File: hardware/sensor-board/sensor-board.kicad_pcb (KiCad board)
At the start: 4 copper layers, 59.2 x 26.5 mm, 44 parts, among them J1 QWIIC Connector, J2 QWIIC Connector, J3 3-pole terminal, J4 2-pole terminal, Q1 BSS84, SW1 SW_DIP_x03, U2 DS2482S-100+, U3 PCA9501PW_118, U4 LMV601, U5 MCP96L01T-E/MX, U6 ADS7823EB/250

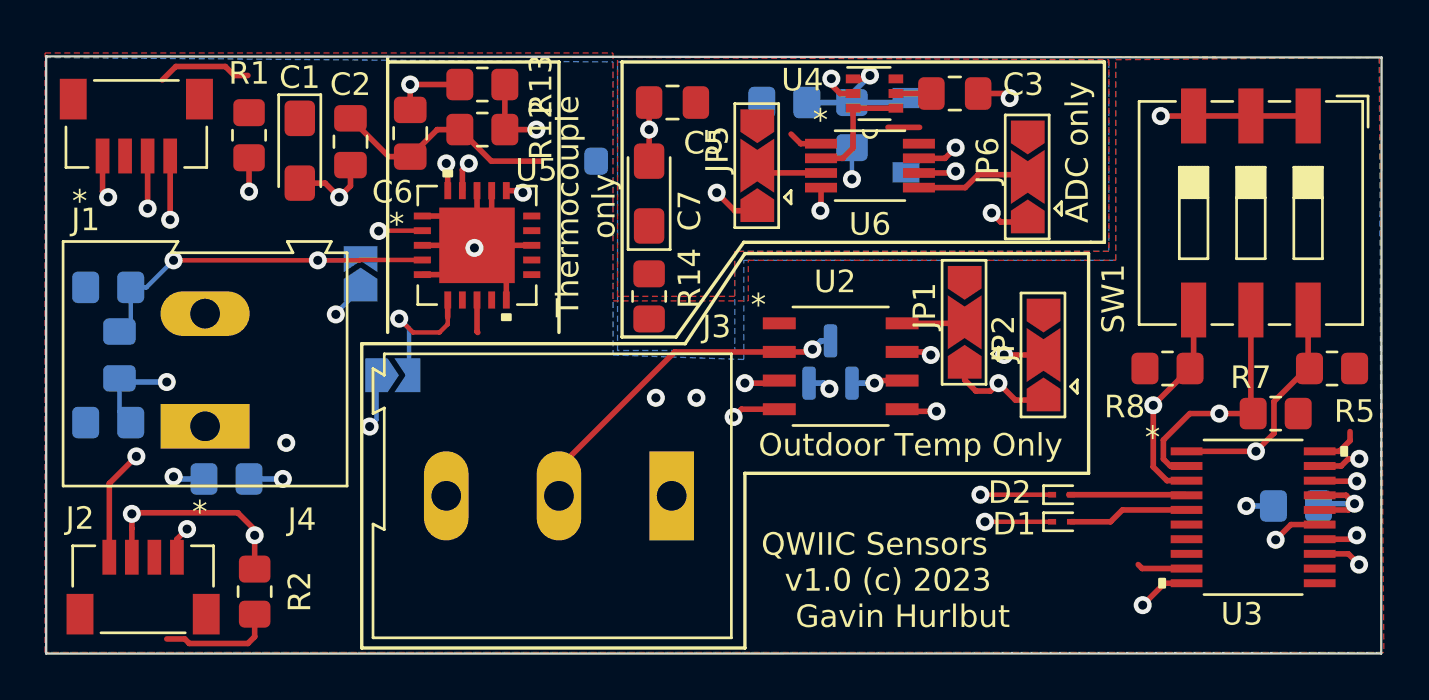
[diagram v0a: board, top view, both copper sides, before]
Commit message: Change coolant sensor to a 10k NTC thermistor
- this requires one more "TBD" resistor to be added to the board.
- regenerated gerbers
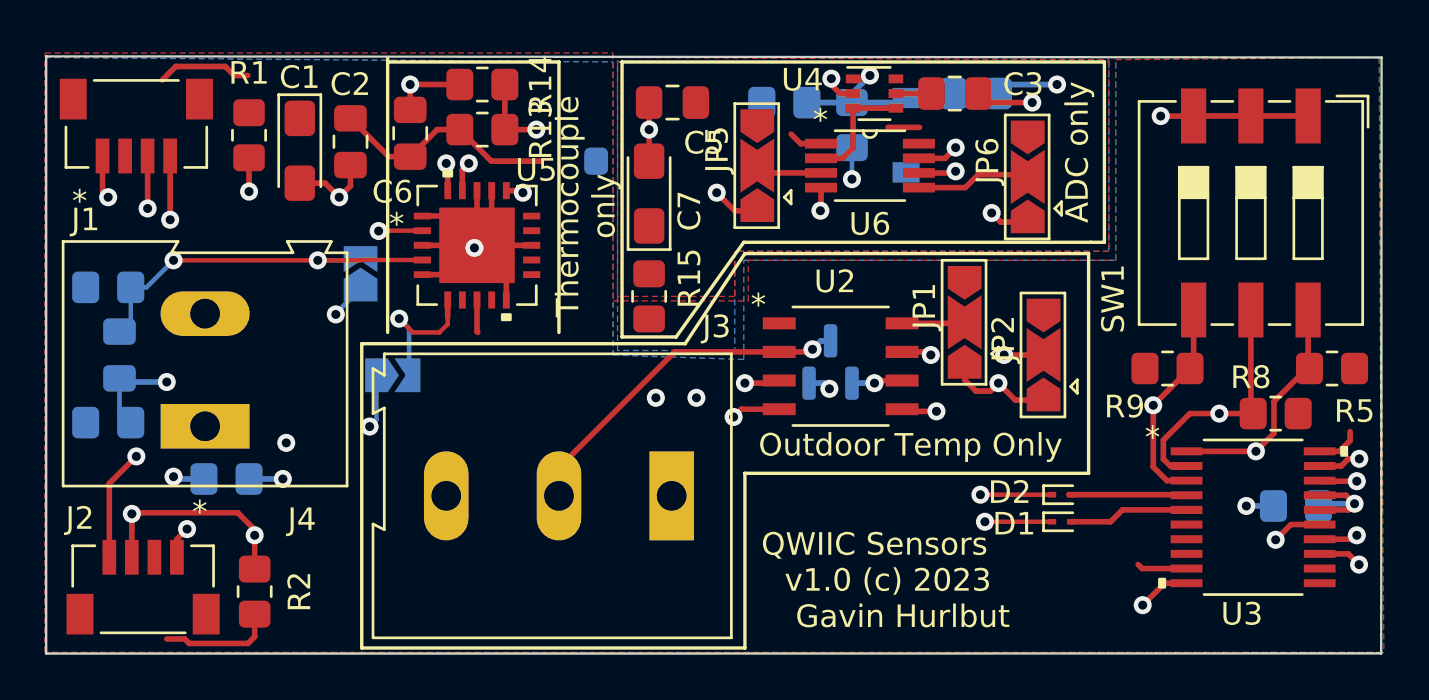
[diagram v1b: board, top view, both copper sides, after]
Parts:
- added R6: TBD, Resistor_SMD:R_0805_2012Metric_Pad1.20x1.40mm_HandSolder, B.Cu at (116.5, 126.4)
- renumbered R9 to R10, R10 to R11, R11 to R12, R12 to R13, R13 to R14, R14 to R15, R6 to R7, R7 to R8, R8 to R9
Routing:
- net +3V3A: track 4.48 -> 7.25 mm, vias 0 -> 1
- net Net-(D3-Pad1): track 6.83 -> 9.01 mm
- net GNDA: track 10.8 -> 11.8 mm
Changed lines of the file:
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@@
   (net 21 "A1")
   (net 22 "A2")
-  (net 23 "Net-(R12-Pad2)")
+  (net 23 "Net-(R13-Pad2)")
   (net 24 "unconnected-(U3-Pad6)")
   (net 25 "unconnected-(U3-Pad7)")
@@
     (property "Sheetname" "")
     (attr smd)
-    (fp_text reference "R7" (at 1.1 1.6) (layer "F.SilkS")
+    (fp_text reference "R8" (at 1.1 1.6) (layer "F.SilkS")
       (effects (font (size 1 1) (thickness 0.15)))
     )
@@
       (net 33 "unconnected-(U5-Pad15)") (pinfunction "ALERT4") (pintype "output+no_connect"))
     (pad "16" smd rect locked (at 1.3 -2.4257) (size 0.3048 0.762) (layers "F.Cu" "F.Paste" "F.Mask")
-      (net 23 "Net-(R12-Pad2)") (pinfunction "ADDR") (pintype "input"))
+      (net 23 "Net-(R13-Pad2)") (pinfunction "ADDR") (pintype "input"))
     (pad "17" smd rect locked (at 0.649999 -2.4257) (size 0.3048 0.762) (layers "F.Cu" "F.Paste" "F.Mask")
       (net 2 "GND") (pinfunction "GND") (pintype "power_in"))
@@
     (property "Sheetname" "")
     (attr smd)
-    (fp_text reference "R12" (at 2.6 0 90) (layer "F.SilkS")
+    (fp_text reference "R13" (at 2.6 0 90) (layer "F.SilkS")
       (effects (font (size 1 1) (thickness 0.15)))
     )
@@
       (net 1 "+3V3") (pintype "passive"))
     (pad "2" smd roundrect (at 1 0) (size 1.2 1.4) (layers "F.Cu" "F.Paste" "F.Mask") (roundrect_rratio 0.2083333333)
-      (net 23 "Net-(R12-Pad2)") (pintype "passive"))
+      (net 23 "Net-(R13-Pad2)") (pintype "passive"))
     (model "${KICAD6_3DMODEL_DIR}/Resistor_SMD.3dshapes/R_0805_2012Metric.wrl"
       (offset (xyz 0 0 0))
@@
     (property "Sheetname" "")
     (attr smd)
-    (fp_text reference "R14" (at 0.8 1.8 90) (layer "F.SilkS")
+    (fp_text reference "R15" (at 0.8 1.8 90) (layer "F.SilkS")
       (effects (font (size 1 1) (thickness 0.15)))
     )
@@
     (property "Sheetname" "")
     (attr smd)
-    (fp_text reference "R8" (at -1.9 1.7) (layer "F.SilkS")
+    (fp_text reference "R9" (at -1.9 1.7) (layer "F.SilkS")
       (effects (font (size 1 1) (thickness 0.15)))
     )
@@
     (property "Sheetname" "")
     (attr smd)
-    (fp_text reference "R13" (at -2.6 0 90) (layer "F.SilkS")
+    (fp_text reference "R14" (at -2.6 0 90) (layer "F.SilkS")
       (effects (font (size 1 1) (thickness 0.15)))
     )
@@
     (fp_line (start -1 0.625) (end -1 -0.625) (layer "F.Fab") (width 0.1))
     (pad "1" smd roundrect (at -1 0 180) (size 1.2 1.4) (layers "F.Cu" "F.Paste" "F.Mask") (roundrect_rratio 0.2083333333)
-      (net 23 "Net-(R12-Pad2)") (pintype "passive"))
+      (net 23 "Net-(R13-Pad2)") (pintype "passive"))
     (pad "2" smd roundrect (at 1 0 180) (size 1.2 1.4) (layers "F.Cu" "F.Paste" "F.Mask") (roundrect_rratio 0.2083333333)
       (net 2 "GND") (pintype "passive"))
@@
     )
   )
+  (footprint "Resistor_SMD:R_0805_2012Metric_Pad1.20x1.40mm_HandSolder" (layer "B.Cu")
+    (at 116.5 126.4 180)
+    (descr "Resistor SMD 0805 (2012 Metric), square (rectangular) end terminal, IPC_7351 nominal with elongated pad for handsoldering. (Body size source: IPC-SM-782 page 72, https://www.pcb-3d.com/wordpress/wp-content/uploads/ipc-sm-782a_amendment_1_and_2.pdf), generated with kicad-footprint-generator")
+    (tags "resistor handsolder")
+    (property "Sheetfile" "sensor-board.kicad_sch")
+    (property "Sheetname" "")
+    (attr smd)
+    (fp_text reference "R6" (at -0.4 -1.8) (layer "B.SilkS")
+      (effects (font (size 1 1) (thickness 0.15)) (justify mirror))
+    )
+    (fp_text value "TBD" (at 0 -1.65) (layer "B.Fab")
+      (effects (font (size 1 1) (thickness 0.15)) (justify mirror))
+    )
+    (fp_text user "${REFERENCE}" (at 0 0) (layer "B.Fab")
+      (effects (font (size 0.5 0.5) (thickness 0.08)) (justify mirror))
+    )
+    (fp_line (start -0.227064 0.735) (end 0.227064 0.735) (layer "B.SilkS") (width 0.12))
+    (fp_line (start -0.227064 -0.735) (end 0.227064 -0.735) (layer "B.SilkS") (width 0.12))
+    (fp_line (start 1.85 -0.95) (end -1.85 -0.95) (layer "B.CrtYd") (width 0.05))
+    (fp_line (start -1.85 0.95) (end 1.85 0.95) (layer "B.CrtYd") (width 0.05))
+    (fp_line (start 1.85 0.95) (end 1.85 -0.95) (layer "B.CrtYd") (width 0.05))
+    (fp_line (start -1.85 -0.95) (end -1.85 0.95) (layer "B.CrtYd") (width 0.05))
+    (fp_line (start 1 0.625) (end 1 -0.625) (layer "B.Fab") (width 0.1))
+    (fp_line (start -1 -0.625) (end -1 0.625) (layer "B.Fab") (width 0.1))
+    (fp_line (start -1 0.625) (end 1 0.625) (layer "B.Fab") (width 0.1))
+    (fp_line (start 1 -0.625) (end -1 -0.625) (layer "B.Fab") (width 0.1))
+    (pad "1" smd roundrect (at -1 0 180) (size 1.2 1.4) (layers "B.Cu" "B.Paste" "B.Mask") (roundrect_rratio 0.208333)
+      (net 6 "+3V3A") (pintype "passive"))
+    (pad "2" smd roundrect (at 1 0 180) (size 1.2 1.4) (layers "B.Cu" "B.Paste" "B.Mask") (roundrect_rratio 0.208333)
+      (net 17 "Net-(D3-Pad1)") (pintype "passive"))
+    (model "${KICAD6_3DMODEL_DIR}/Resistor_SMD.3dshapes/R_0805_2012Metric.wrl"
+      (offset (xyz 0 0 0))
+      (scale (xyz 1 1 1))
+      (rotate (xyz 0 0 0))
+    )
+  )
   (footprint "Jumper:SolderJumper-2_P1.3mm_Open_TrianglePad1.0x1.5mm" (layer "B.Cu")
     (at 89.2 134.4 90)
@@
     (property "Sheetname" "")
     (attr smd)
-    (fp_text reference "R10" (at 0.75 -1.75) (layer "B.SilkS")
+    (fp_text reference "R11" (at 0.75 -1.75) (layer "B.SilkS")
       (effects (font (size 1 1) (thickness 0.15)) (justify mirror))
     )
@@
     (property "Sheetname" "")
     (attr smd)
-    (fp_text reference "R11" (at -3 0.25) (layer "B.SilkS")
+    (fp_text reference "R12" (at -3 0.25) (layer "B.SilkS")
       (effects (font (size 1 1) (thickness 0.15)) (justify mirror))
     )
@@
     (property "Sheetname" "")
     (attr smd)
-    (fp_text reference "R9" (at -0.65 -1.6 180) (layer "B.SilkS")
+    (fp_text reference "R10" (at -0.65 -1.6 180) (layer "B.SilkS")
       (effects (font (size 1 1) (thickness 0.15)) (justify mirror))
     )
@@
     (property "Sheetname" "")
     (attr smd)
-    (fp_text reference "R6" (at 1 -1.8) (layer "B.SilkS")
+    (fp_text reference "R7" (at 1 -1.8) (layer "B.SilkS")
       (effects (font (size 1 1) (thickness 0.15)) (justify mirror))
     )
@@
   (segment (start 102 127.2375) (end 101.7625 127) (width 0.25) (layer "F.Cu") (net 5))
   (segment (start 118.8 132.1) (end 117.6 132.1) (width 0.25) (layer "F.Cu") (net 5))
+  (segment (start 117 126.8) (end 116.6 126.4) (width 0.25) (layer "F.Cu") (net 5))
   (segment (start 109.6283 130.574999) (end 109.6283 131.5717) (width 0.25) (layer "F.Cu") (net 5))
   (segment (start 110.475 126.4) (end 110.085493 126.010493) (width 0.25) (layer "F.Cu") (net 5))
-  (segment (start 116.6 126.4) (end 117.8 126.4) (width 0.25) (layer "F.Cu") (net 5))
   (segment (start 105.8 131.6) (end 105 130.8) (width 0.25) (layer "F.Cu") (net 5))
   (segment (start 117.6 132.1) (end 117.2 131.7) (width 0.25) (layer "F.Cu") (net 5))
@@
   (segment (start 111.05 126.4) (end 110.475 126.4) (width 0.25) (layer "F.Cu") (net 5))
   (segment (start 110.085493 126.010493) (end 110.085493 125.738744) (width 0.25) (layer "F.Cu") (net 5))
-  (segment (start 117.8 126.4) (end 118 126.6) (width 0.25) (layer "F.Cu") (net 5))
+  (segment (start 119 126.8) (end 117 126.8) (width 0.25) (layer "F.Cu") (net 5))
   (via (at 117.2 131.7) (size 0.8) (drill 0.4) (layers "F.Cu" "B.Cu") (net 5))
   (via (at 102 128) (size 0.8) (drill 0.4) (layers "F.Cu" "B.Cu") (net 5))
   (via (at 105 130.8) (size 0.8) (drill 0.4) (layers "F.Cu" "B.Cu") (net 5))
   (via (at 110.085493 125.738744) (size 0.8) (drill 0.4) (layers "F.Cu" "B.Cu") (net 5))
-  (via (at 118 126.6) (size 0.8) (drill 0.4) (layers "F.Cu" "B.Cu") (net 5))
+  (via (at 119 126.8) (size 0.8) (drill 0.4) (layers "F.Cu" "B.Cu") (net 5))
   (via (at 109.6 131.6) (size 0.8) (drill 0.4) (layers "F.Cu" "B.Cu") (net 5))
   (segment locked (start 108.725001 128.625001) (end 108.3 128.2) (width 0.25) (layer "F.Cu") (net 6))
@@
   (segment locked (start 112.6 127.9) (end 114 127.9) (width 0.25) (layer "F.Cu") (net 6))
   (segment locked (start 112.95 126.4) (end 114.525 126.4) (width 0.25) (layer "F.Cu") (net 6))
+  (via (at 120.1 126) (size 0.8) (drill 0.4) (layers "F.Cu" "B.Cu") (net 6))
+  (segment (start 117.5 126.4) (end 117.9 126) (width 0.25) (layer "B.Cu") (net 6))
+  (segment (start 117.9 126) (end 120.1 126) (width 0.25) (layer "B.Cu") (net 6))
   (segment (start 93.065 136.635) (end 93.065 136.335) (width 0.2) (layer "F.Cu") (net 7))
   (segment (start 90.912299 136.387701) (end 91.524598 137) (width 0.2) (layer "F.Cu") (net 7))
@@
   (segment (start 111.65 125.75) (end 111.05 125.75) (width 0.25) (layer "F.Cu") (net 17))
   (via (at 111.8 125.6) (size 0.8) (drill 0.4) (layers "F.Cu" "B.Cu") (net 17))
+  (segment (start 113.4 126.6) (end 115.3 126.6) (width 0.25) (layer "B.Cu") (net 17))
   (segment (start 111 126.4) (end 111.8 125.6) (width 0.25) (layer "B.Cu") (net 17))
+  (segment (start 115.3 126.6) (end 115.5 126.4) (width 0.25) (layer "B.Cu") (net 17))
   (segment (start 111 126.8) (end 111 126.4) (width 0.25) (layer "B.Cu") (net 17))
   (segment (start 113.2 126.8) (end 113.4 126.6) (width 0.25) (layer "B.Cu") (net 17))

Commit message: Changed DIP switch to solder jumper pads, regen gerbers
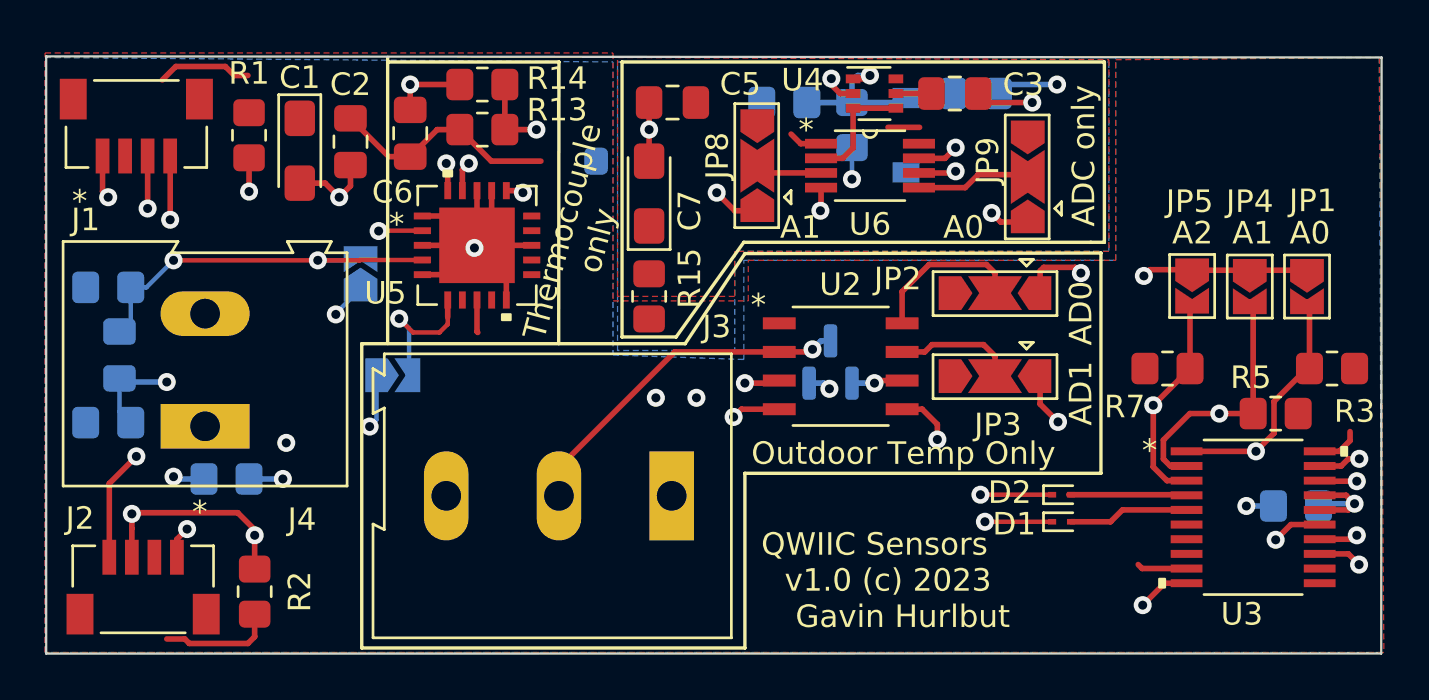
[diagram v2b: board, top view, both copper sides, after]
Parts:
- removed SW1: SW_DIP_x03, Button_Switch_SMD:SW_DIP_SPSTx03_Slide_9.78x9.8mm_W8.61mm_P2.54mm
- added JP1: Solder Jumper, Jumper:SolderJumper-2_P1.3mm_Open_TrianglePad1.0x1.5mm, F.Cu at (131.2, 135.0)
- added JP4: Solder Jumper, Jumper:SolderJumper-2_P1.3mm_Open_TrianglePad1.0x1.5mm, F.Cu at (128.7, 135.0)
- added JP5: Solder Jumper, Jumper:SolderJumper-2_P1.3mm_Open_TrianglePad1.0x1.5mm, F.Cu at (126.1, 134.9)
- moved JP3 2.35 mm to (117.3, 138.9), turned to 180 degrees
- moved JP2 1.87 mm to (117.3, 135.3), turned to 180 degrees
- renumbered JP1 to JP2, JP2 to JP3, JP3 to JP6, JP4 to JP7, JP5 to JP8, JP6 to JP9, R5 to R3, R3 to R4, R8 to R5, R4 to R6, R9 to R7, R6 to R8, R7 to R9
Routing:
- net Net-(JP2-Pad2): track 2.79 -> 7.08 mm
- net GND: track 44.6 -> 45.9 mm, vias 9 -> 10
- net SDA: track 111.7 -> 112.8 mm
- net Net-(JP3-Pad2): track 6.33 -> 5.36 mm, vias 2 -> 0
- net A2: track 20.5 -> 21.0 mm
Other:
- board text added: "A0"
- board text added: "A1"
- board text added: "A2"
- board text added: "AD0"
- board text added: "AD1"
- board text added: "VIN+"
- board text added: "VIN-"

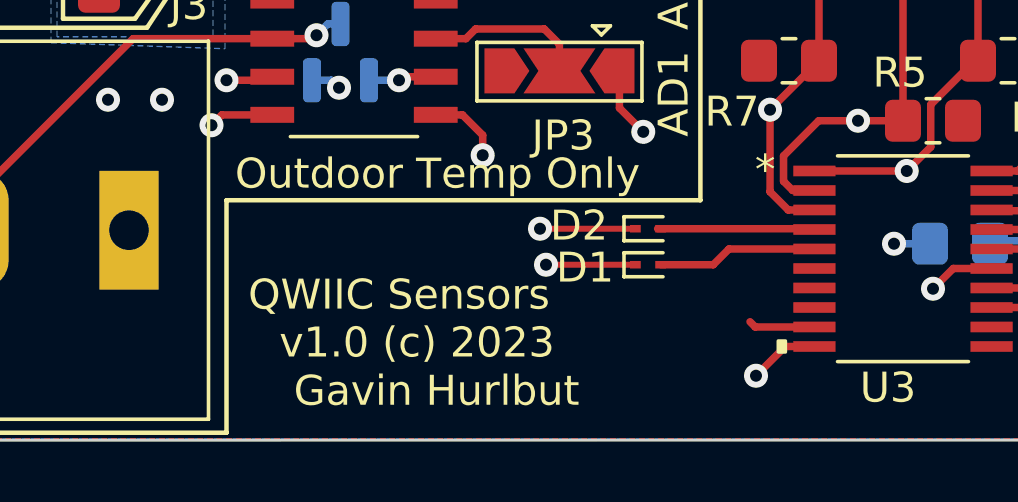
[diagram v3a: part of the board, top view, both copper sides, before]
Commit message: Got rid of TINY diode (0402!?!?), remove USE_USB, put in PicoW
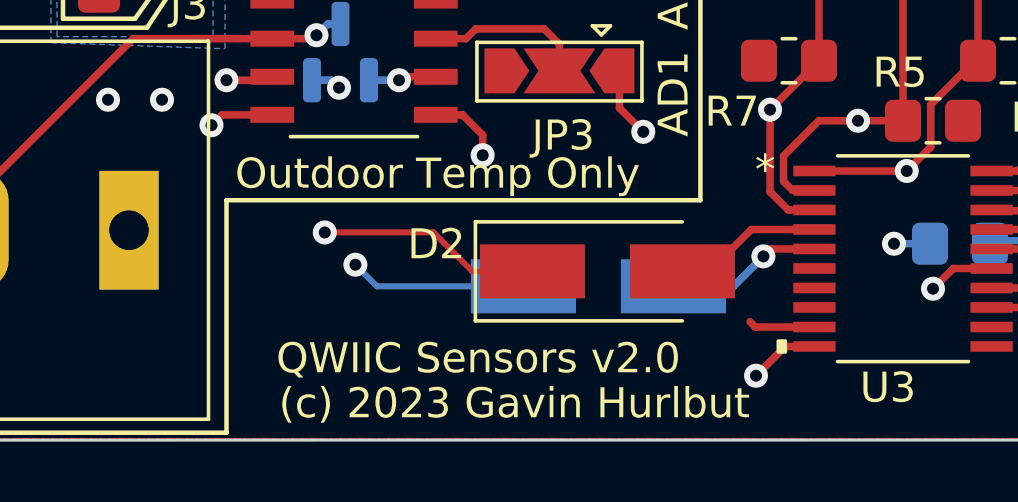
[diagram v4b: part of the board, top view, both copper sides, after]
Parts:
- D1: value ACDBQC0130L-HF -> BYS10-35; footprint Diode_SMD:D_SOD-923 -> Diode_SMD:D_SMA_Handsoldering; moved to B.Cu
- D2: value ACDBQC0130L-HF -> BYS10-35; footprint Diode_SMD:D_SOD-923 -> Diode_SMD:D_SMA_Handsoldering
- moved REF** 24.4 mm to (128.2, 129.0)
- moved D2 1.96 mm to (118.9, 145.6)
- moved D1 1.80 mm to (118.6, 146.1)
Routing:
- net VIN+: track 57.6 -> 54.1 mm
- net VIN-: track 42.6 -> 39.8 mm
- net Net-(U3-Pad5): track 5.34 -> 5.22 mm, vias 0 -> 1
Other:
- board text added: "(c) 2023 Gavin Hurlbut"
- board text added: "QWIIC Sensors v2.0"
- board text removed: "QWIIC Sensors"
- board text removed: "v1.0 (c) 2023 Gavin Hurlbut"
